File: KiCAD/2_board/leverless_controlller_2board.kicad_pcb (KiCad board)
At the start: 2 copper layers, 208.5 x 127.2 mm, 80 parts, among them J1 USB_C_Receptacle_USB2.0_14P, J2 Conn_01x03_Socket, J3 Conn_01x06_Socket, J4 Conn_01x06_Socket, J7 Conn_01x06_Socket, J8 Conn_01x06_Socket, SW1 Memory Reset, SW10_SHARE1 SW_Push, SW11_START1 SW_Push, SW12_THROW1 SW_Push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

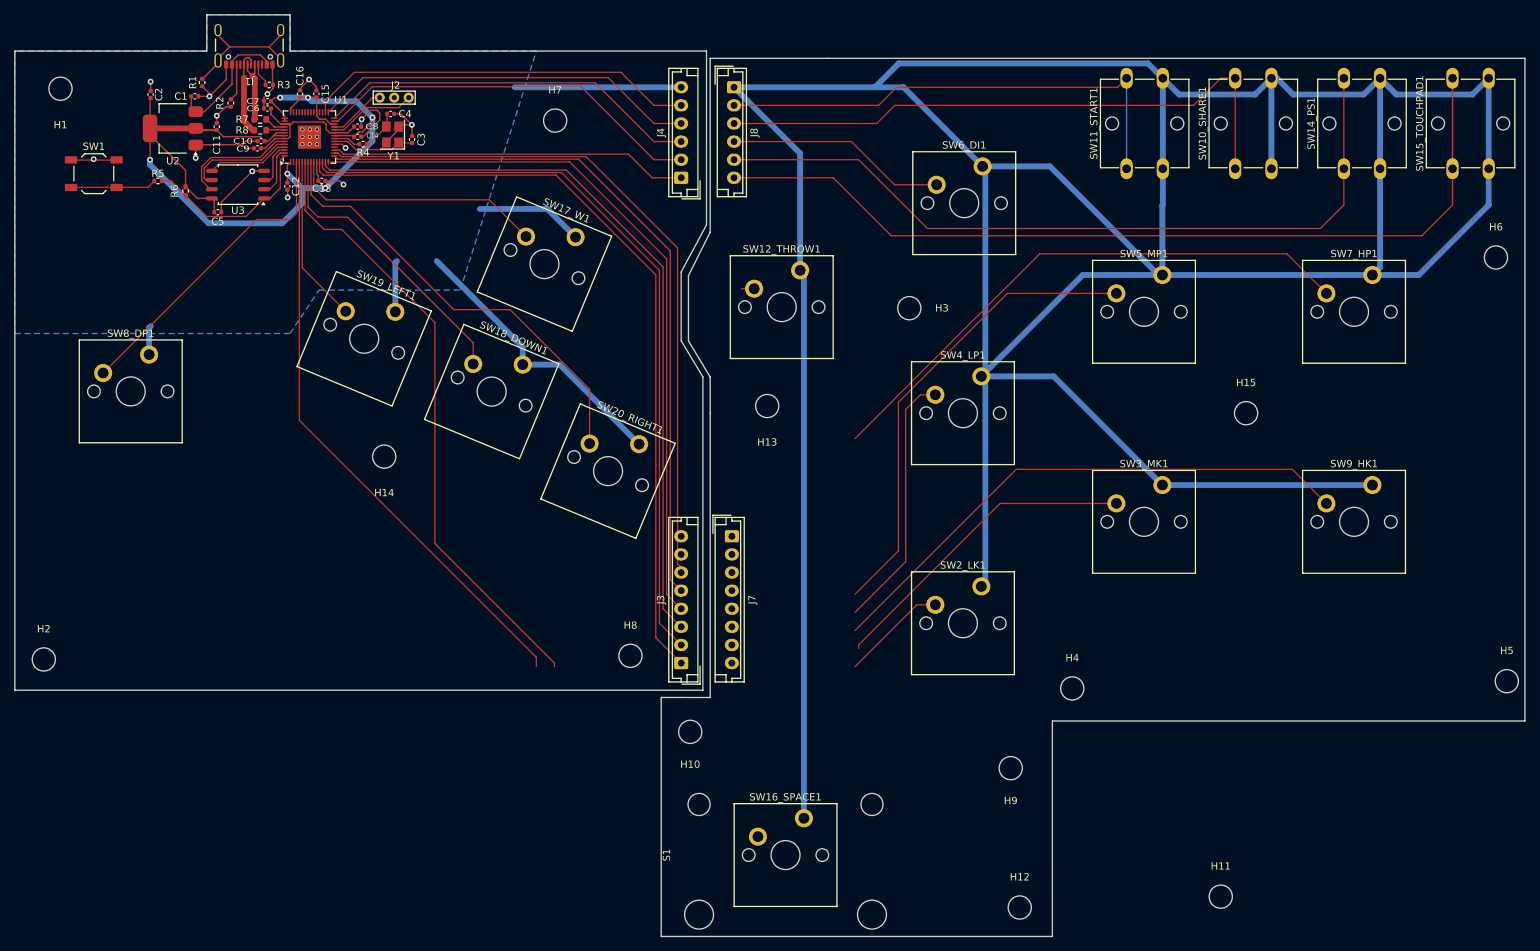
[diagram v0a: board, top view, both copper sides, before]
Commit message: Panelize 4 board design
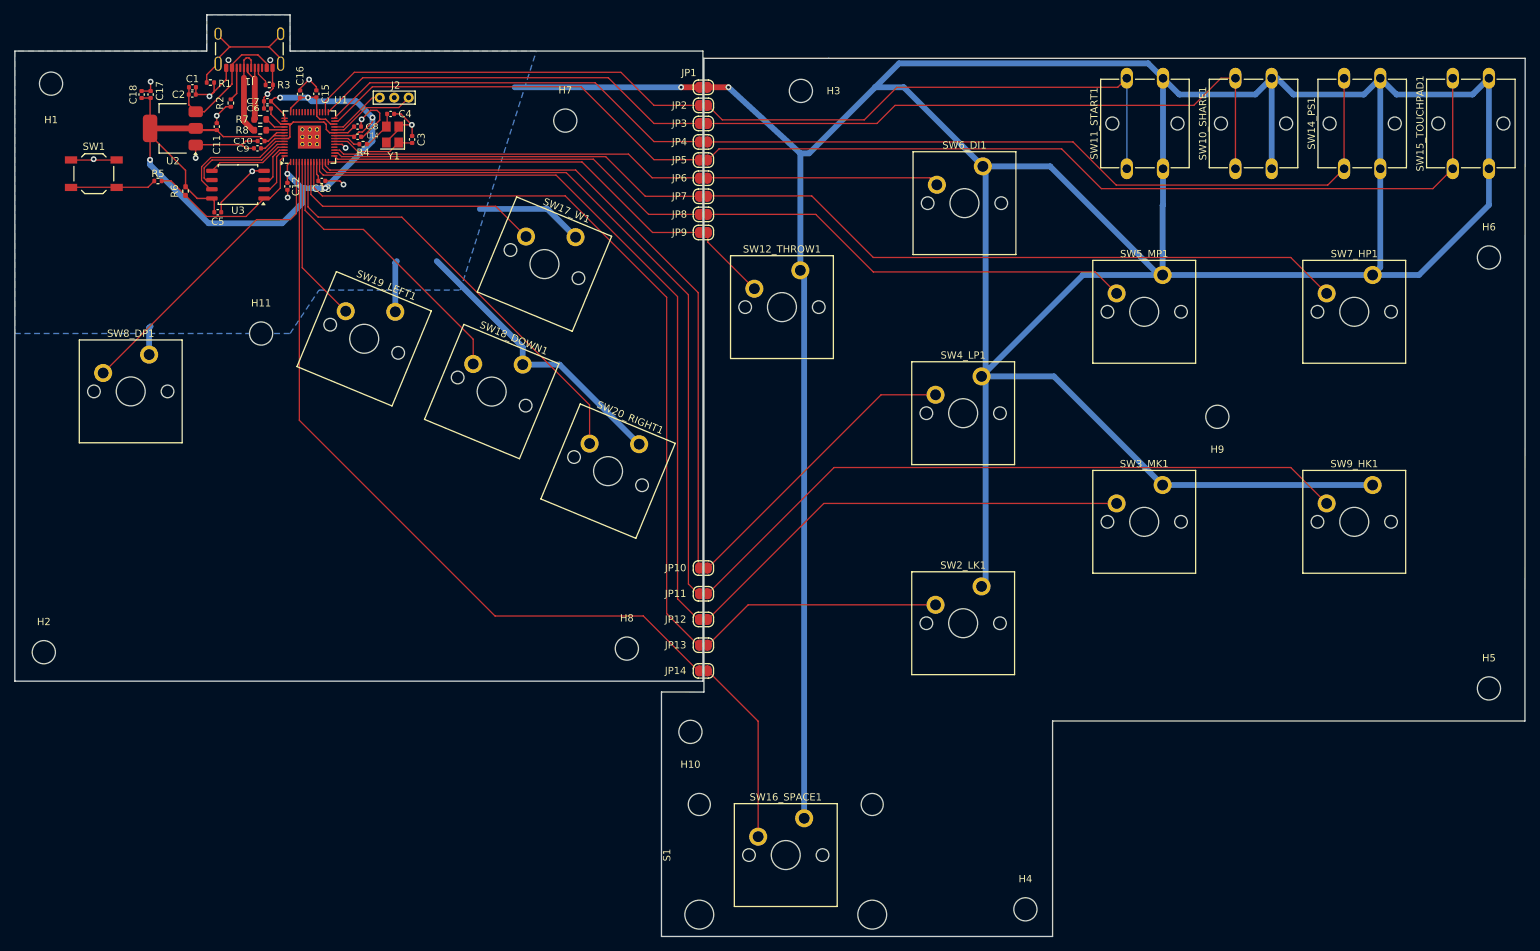
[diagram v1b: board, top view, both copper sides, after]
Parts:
- removed H12, H13, H14, H15: MountingHole, MountingHole:MountingHole_3.2mm_M3
- removed J3, J7: Conn_01x06_Socket, Connector_JST:JST_EH_B8B-EH-A_1x08_P2.50mm_Vertical
- removed J4, J8: Conn_01x06_Socket, Connector_JST:JST_EH_B6B-EH-A_1x06_P2.50mm_Vertical
- added C1: 4.7u, Capacitor_SMD:C_0402_1005Metric, F.Cu at (68.5, 30.0)
- added C18: 4.7u, Capacitor_SMD:C_0402_1005Metric, F.Cu at (61.5, 31.0)
- added JP1: SolderJumper_2_Bridged, Fightstick_Library:EdgeSolderJumper-2_P1.3mm_Bridged_RoundedPad1.0x1.5mm, F.Cu at (139.1, 30.0)
- added JP10: SolderJumper_2_Bridged, Fightstick_Library:EdgeSolderJumper-2_P1.3mm_Bridged_RoundedPad1.0x1.5mm, F.Cu at (139.1, 96.4)
- added JP11: SolderJumper_2_Bridged, Fightstick_Library:EdgeSolderJumper-2_P1.3mm_Bridged_RoundedPad1.0x1.5mm, F.Cu at (139.1, 99.9)
- added JP12: SolderJumper_2_Bridged, Fightstick_Library:EdgeSolderJumper-2_P1.3mm_Bridged_RoundedPad1.0x1.5mm, F.Cu at (139.1, 103.5)
- added JP13: SolderJumper_2_Bridged, Fightstick_Library:EdgeSolderJumper-2_P1.3mm_Bridged_RoundedPad1.0x1.5mm, F.Cu at (139.1, 107.0)
- added JP14: SolderJumper_2_Bridged, Fightstick_Library:EdgeSolderJumper-2_P1.3mm_Bridged_RoundedPad1.0x1.5mm, F.Cu at (139.1, 110.6)
- added JP2: SolderJumper_2_Bridged, Fightstick_Library:EdgeSolderJumper-2_P1.3mm_Bridged_RoundedPad1.0x1.5mm, F.Cu at (139.1, 32.5)
- added JP3: SolderJumper_2_Bridged, Fightstick_Library:EdgeSolderJumper-2_P1.3mm_Bridged_RoundedPad1.0x1.5mm, F.Cu at (139.1, 35.0)
- added JP4: SolderJumper_2_Bridged, Fightstick_Library:EdgeSolderJumper-2_P1.3mm_Bridged_RoundedPad1.0x1.5mm, F.Cu at (139.1, 37.5)
- added JP5: SolderJumper_2_Bridged, Fightstick_Library:EdgeSolderJumper-2_P1.3mm_Bridged_RoundedPad1.0x1.5mm, F.Cu at (139.1, 40.0)
- added JP6: SolderJumper_2_Bridged, Fightstick_Library:EdgeSolderJumper-2_P1.3mm_Bridged_RoundedPad1.0x1.5mm, F.Cu at (139.1, 42.5)
- added JP7: SolderJumper_2_Bridged, Fightstick_Library:EdgeSolderJumper-2_P1.3mm_Bridged_RoundedPad1.0x1.5mm, F.Cu at (139.1, 45.0)
- added JP8: SolderJumper_2_Bridged, Fightstick_Library:EdgeSolderJumper-2_P1.3mm_Bridged_RoundedPad1.0x1.5mm, F.Cu at (139.1, 47.5)
- added JP9: SolderJumper_2_Bridged, Fightstick_Library:EdgeSolderJumper-2_P1.3mm_Bridged_RoundedPad1.0x1.5mm, F.Cu at (139.1, 50.0)
- J1: footprint Leverless_Controller_Library:USB_C_Receptacle_C6332272 -> Fightstick_Library:USB_C_Receptacle_U262-161N-4BVC11
- J2: footprint Leverless_Controller_Library:Debug_Points -> Fightstick_Library:Debug_Points
- moved H11 153.6 mm to (78.0, 64.0)
- moved H9 56.3 mm to (210.0, 75.5)
- moved H3 33.5 mm to (152.5, 30.5)
- moved H4 31.2 mm to (183.5, 143.5)
- moved H5 2.66 mm to (247.5, 113.0)
- moved H1 1.48 mm to (49.0, 29.5)
- moved H7 1.40 mm to (120.0, 34.6)
- moved R1 1.14 mm to (71.0, 29.3), turned to 0 degrees
- moved H8 1.12 mm to (128.5, 107.5)
- moved B2 1.00 mm to (158.5, 26.0)
- moved H2 1.00 mm to (48.0, 108.0)
- moved H6 0.97 mm to (247.5, 53.5)
- moved C2 0.42 mm to (68.5, 31.0)
- renumbered C2 to C17, C1 to C2
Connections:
- SW10_SHARE1 pad 1: S1 -> /Buttons/S1
- SW11_START1 pad 1: S2 -> /Buttons/S2
- SW12_THROW1 pad 1: L3 -> /Buttons/L3
- SW14_PS1 pad 1: A1 -> /Buttons/A1
- SW15_TOUCHPAD1 pad 1: A2 -> /Buttons/A2
- SW16_SPACE1 pad 1: SPACE -> /Buttons/SPACE
- SW2_LK1 pad 1: B1 -> /Buttons/B1
- SW3_MK1 pad 1: B2 -> /Buttons/B2
- SW4_LP1 pad 1: B3 -> /Buttons/B3
- SW5_MP1 pad 1: B4 -> /Buttons/B4
- SW6_DI1 pad 1: L1 -> /Buttons/L1
- SW7_HP1 pad 1: R1 -> /Buttons/R1
- SW9_HK1 pad 1: R2 -> /Buttons/R2
- U1 pad 11: B2 -> /Main/B2
- U1 pad 12: R2 -> /Main/R2
- U1 pad 13: B3 -> /Main/B3
- U1 pad 14: L3 -> /Main/L3
- U1 pad 15: B4 -> /Main/B4
- U1 pad 16: R1 -> /Main/R1
- U1 pad 17: L1 -> /Main/L1
- U1 pad 27: A1 -> /Main/A2
- U1 pad 28: A2 -> /Main/A1
- U1 pad 29: S1 -> /Main/S1
- U1 pad 30: S2 -> /Main/S2
- U1 pad 4: LEFT -> /Main/SPACE
- U1 pad 5: DOWN -> LEFT
- U1 pad 6: RIGHT -> DOWN
- U1 pad 7: SPACE -> RIGHT
- U1 pad 9: B1 -> /Main/B1
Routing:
- net (no net): track 1293.5 -> 0.00 mm
- net /Buttons/A2: track 0.00 -> 119.4 mm
- net /Main/B1: track 0.00 -> 108.4 mm
- net /Main/SPACE: track 0.00 -> 105.1 mm
- net /Buttons/A1: track 0.00 -> 103.7 mm
- net /Main/B2: track 0.00 -> 103.6 mm
- net /Main/R2: track 0.00 -> 100.5 mm
- net /Main/B3: track 0.00 -> 97.3 mm
- net /Buttons/R2: track 0.00 -> 94.7 mm
- net /Buttons/R1: track 0.00 -> 91.0 mm
- net /Buttons/S1: track 0.00 -> 87.9 mm
- net RIGHT: track 147.0 -> 61.7 mm
- net LEFT: track 106.3 -> 23.1 mm
- net R1: track 77.9 -> 0.00 mm
- net R2: track 76.3 -> 0.00 mm
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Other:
- outline, holes or cut-outs redrawn
